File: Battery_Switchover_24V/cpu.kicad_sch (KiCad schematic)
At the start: 36 parts, among them J1 USB_C_Receptacle_USB2.0_14P, M1 Fan, Q1 PZT2222AT1G, SW1 SW_Push, U14 OPA2197xD, U3 LPC11U14FBD48-201, Y1 12.000MHz

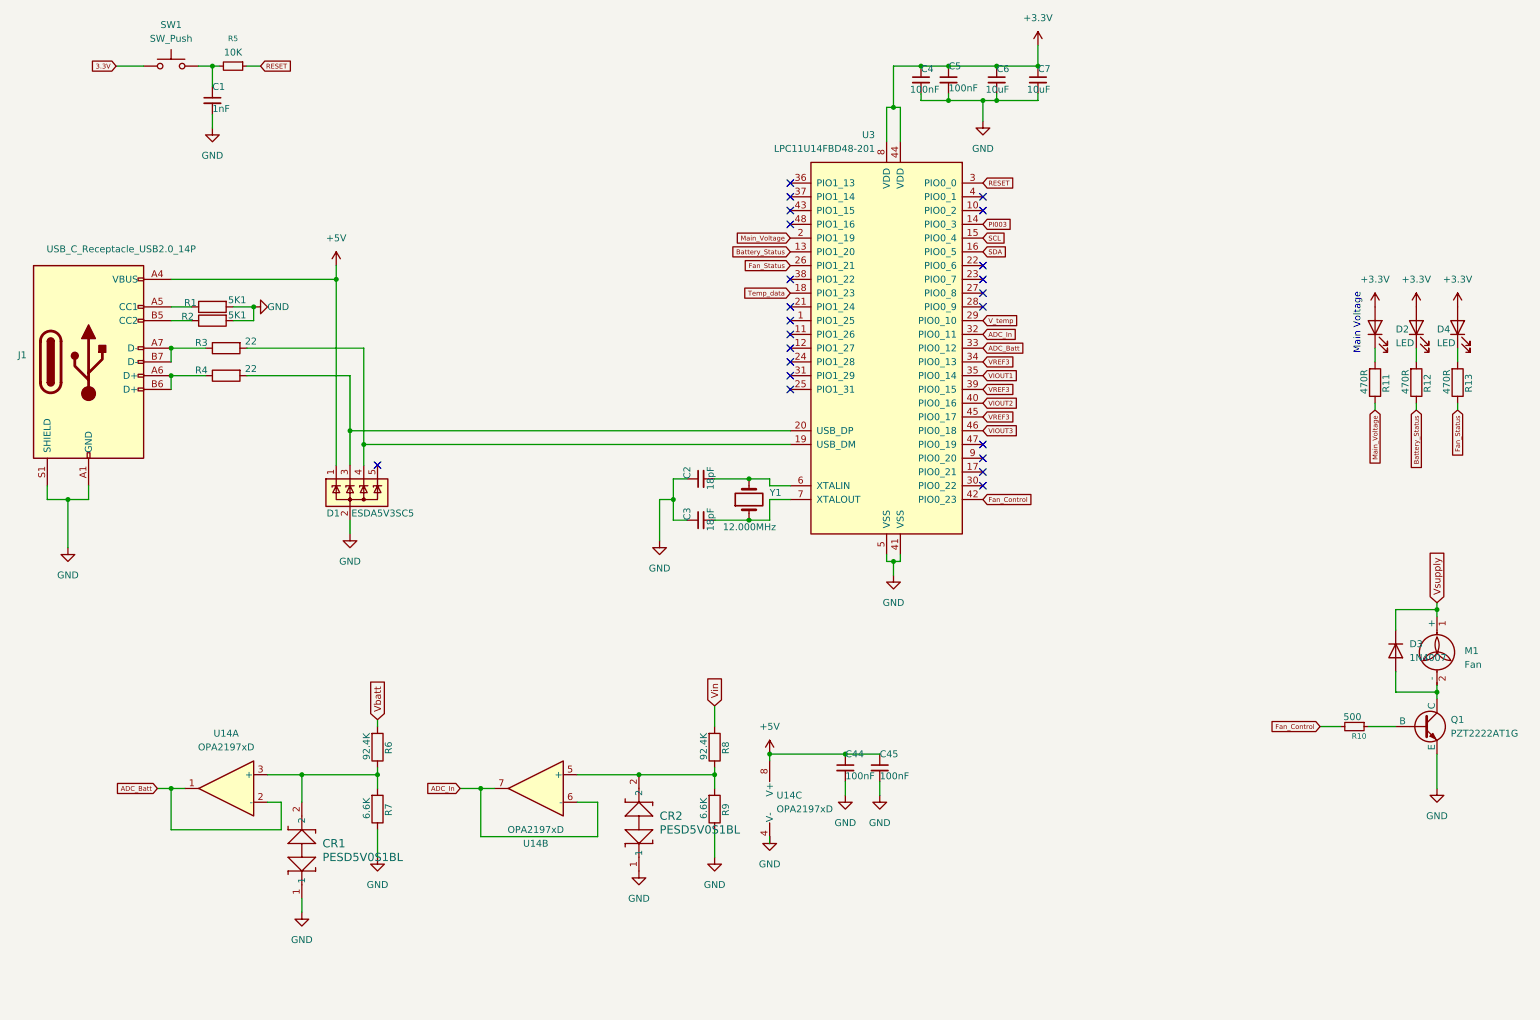
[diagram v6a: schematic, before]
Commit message: Schematics small changes on CPU page
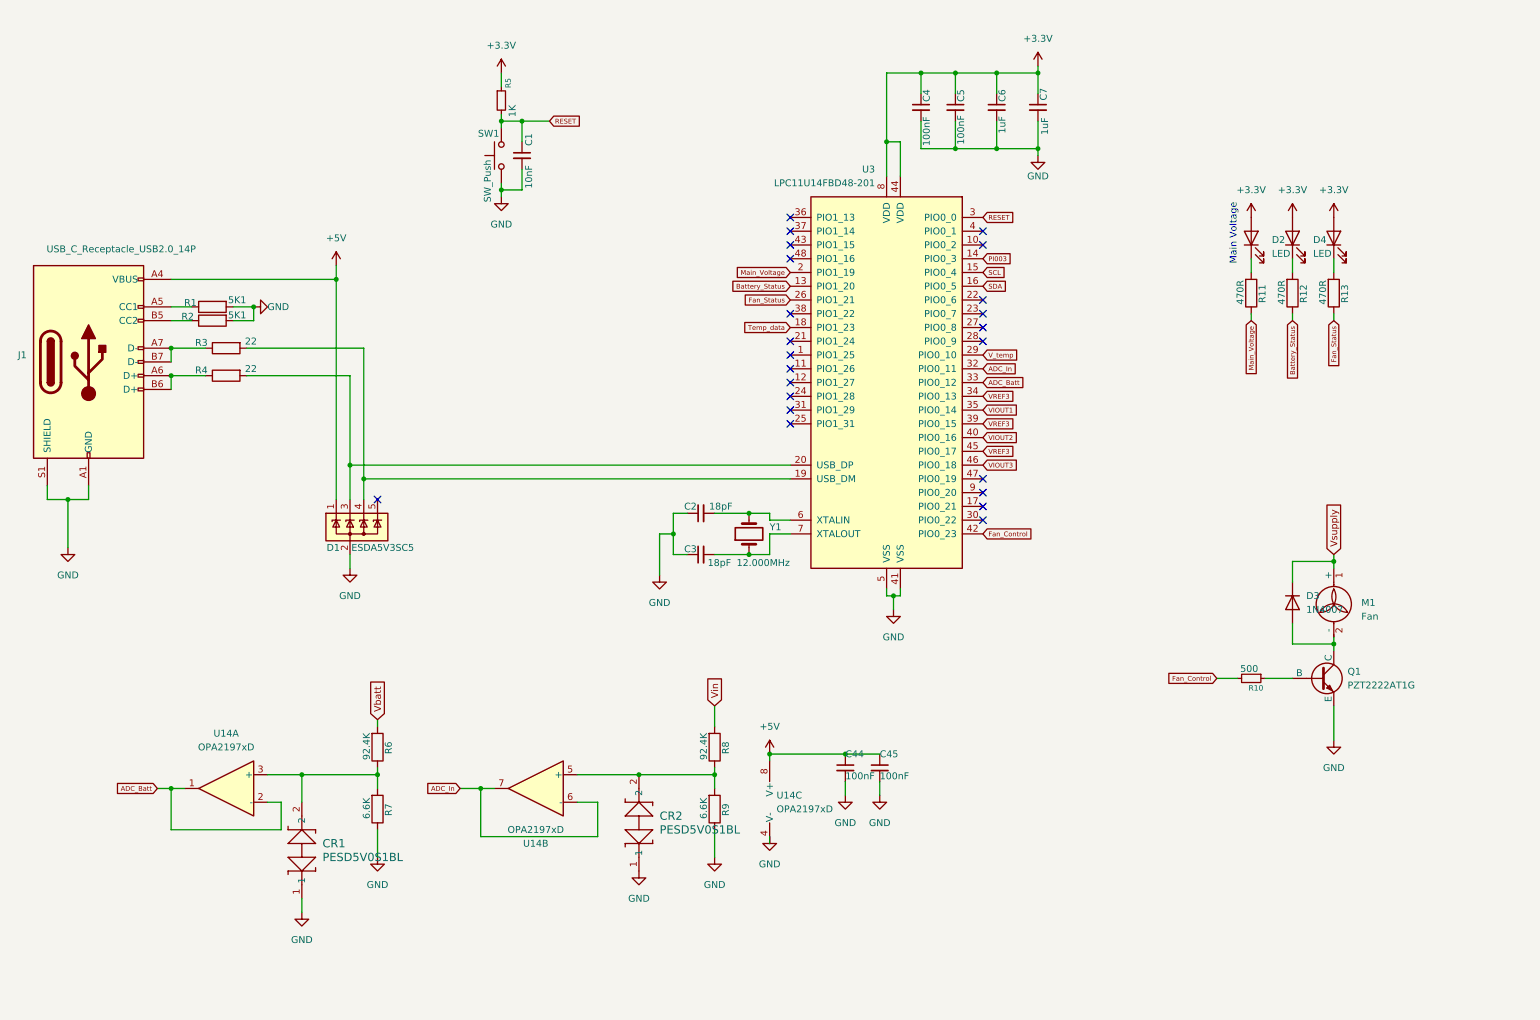
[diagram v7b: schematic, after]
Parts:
- C1: value 1nF -> 10nF
- C6, C7: value 10uF -> 1uF
- R5: value 10K -> 1K
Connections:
- net 3.3V is gone; now on net GND: SW1.1
- net +3.3V: now also R5.1
- net RESET: now also C1.1, R5.2, SW1.2; no longer R5.1
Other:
- moved on the sheet: C1, C2, C3, C4, C5, C6, C7, D1, D2, D3, D4, M1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

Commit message: aded bms details
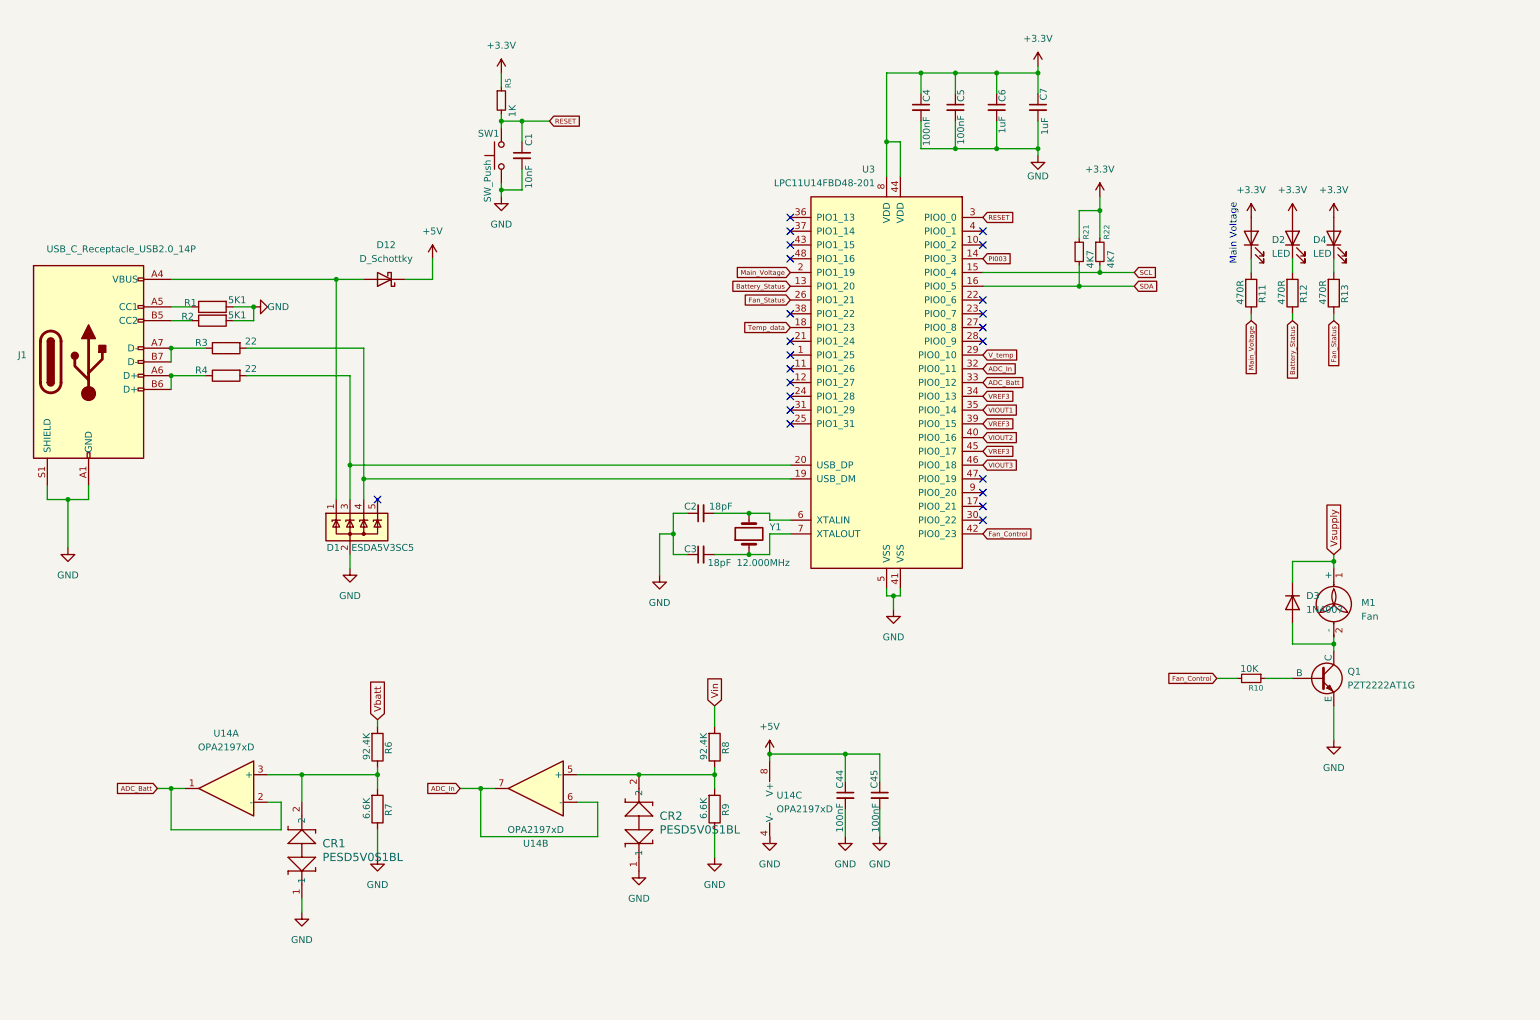
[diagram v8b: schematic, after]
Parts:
- added D12: D_Schottky, symbol Device:D_Schottky
- added R21, R22: 4K7, Resistor_SMD:R_0603_1608Metric, symbol Device:R_Small
- R10: value 500 -> 10K
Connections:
- net +3.3V: now also R21.1, R22.1
- net +5V: now also D12.1 (K); no longer D1.1 (K), J1.A4 (VBUS), J1.A9 (VBUS), J1.B4 (VBUS), J1.B9 (VBUS)
- net SCL: now also R22.2
- net SDA: now also R21.2
- new net: D1.1 (K), D12.2 (A), J1.A4 (VBUS), J1.A9 (VBUS), J1.B4 (VBUS), J1.B9 (VBUS)
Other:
- moved on the sheet: C44, C45
